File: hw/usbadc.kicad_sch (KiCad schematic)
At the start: 0 parts

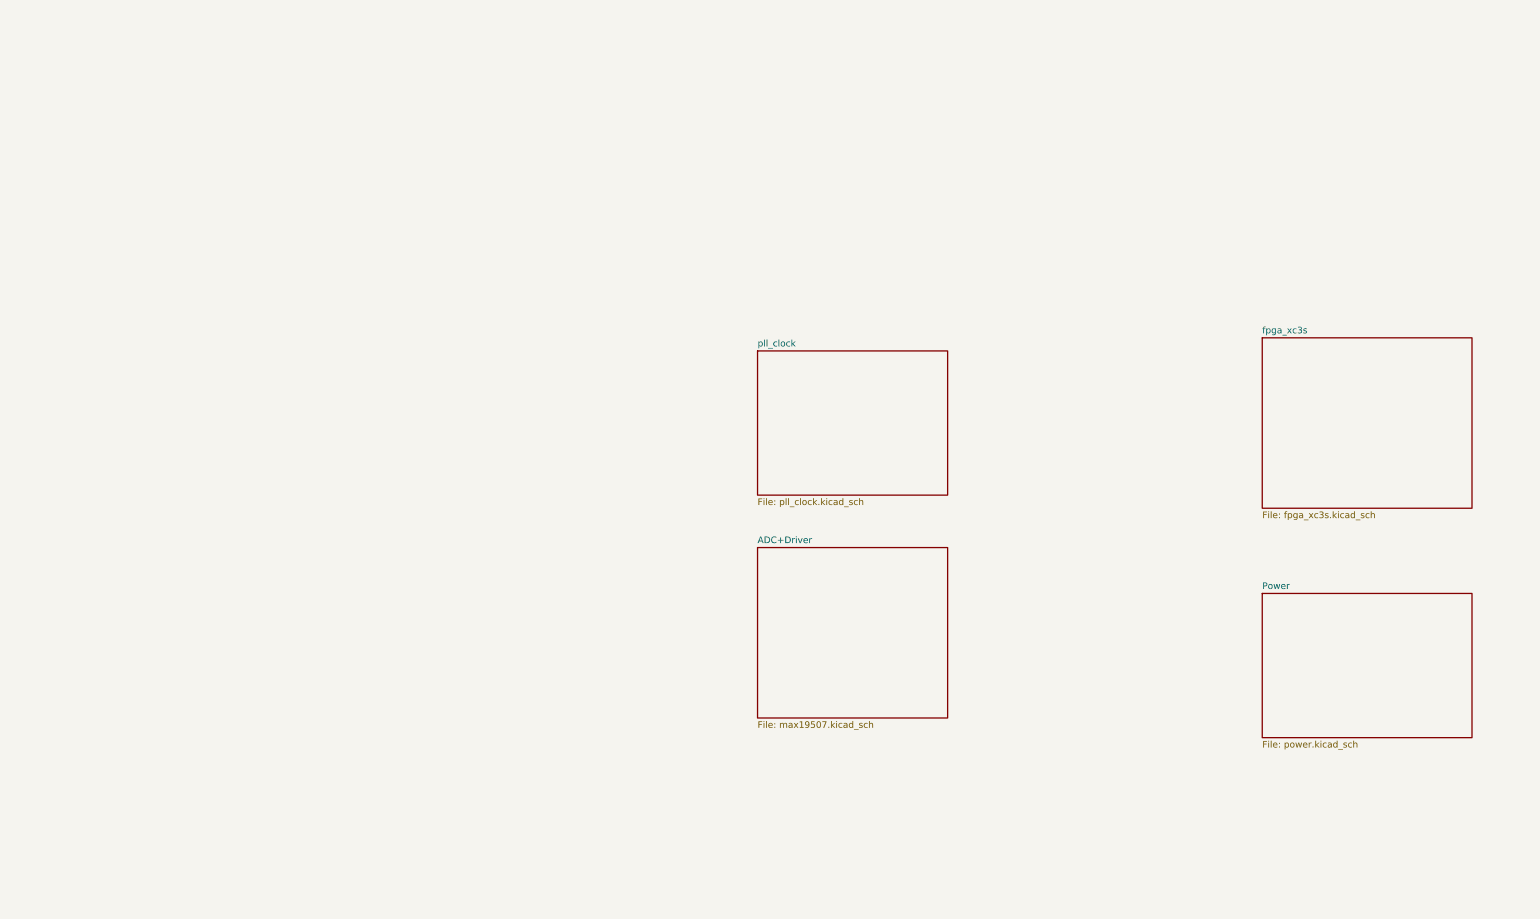
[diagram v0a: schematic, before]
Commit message: basic schematic, started layout (placing first components)
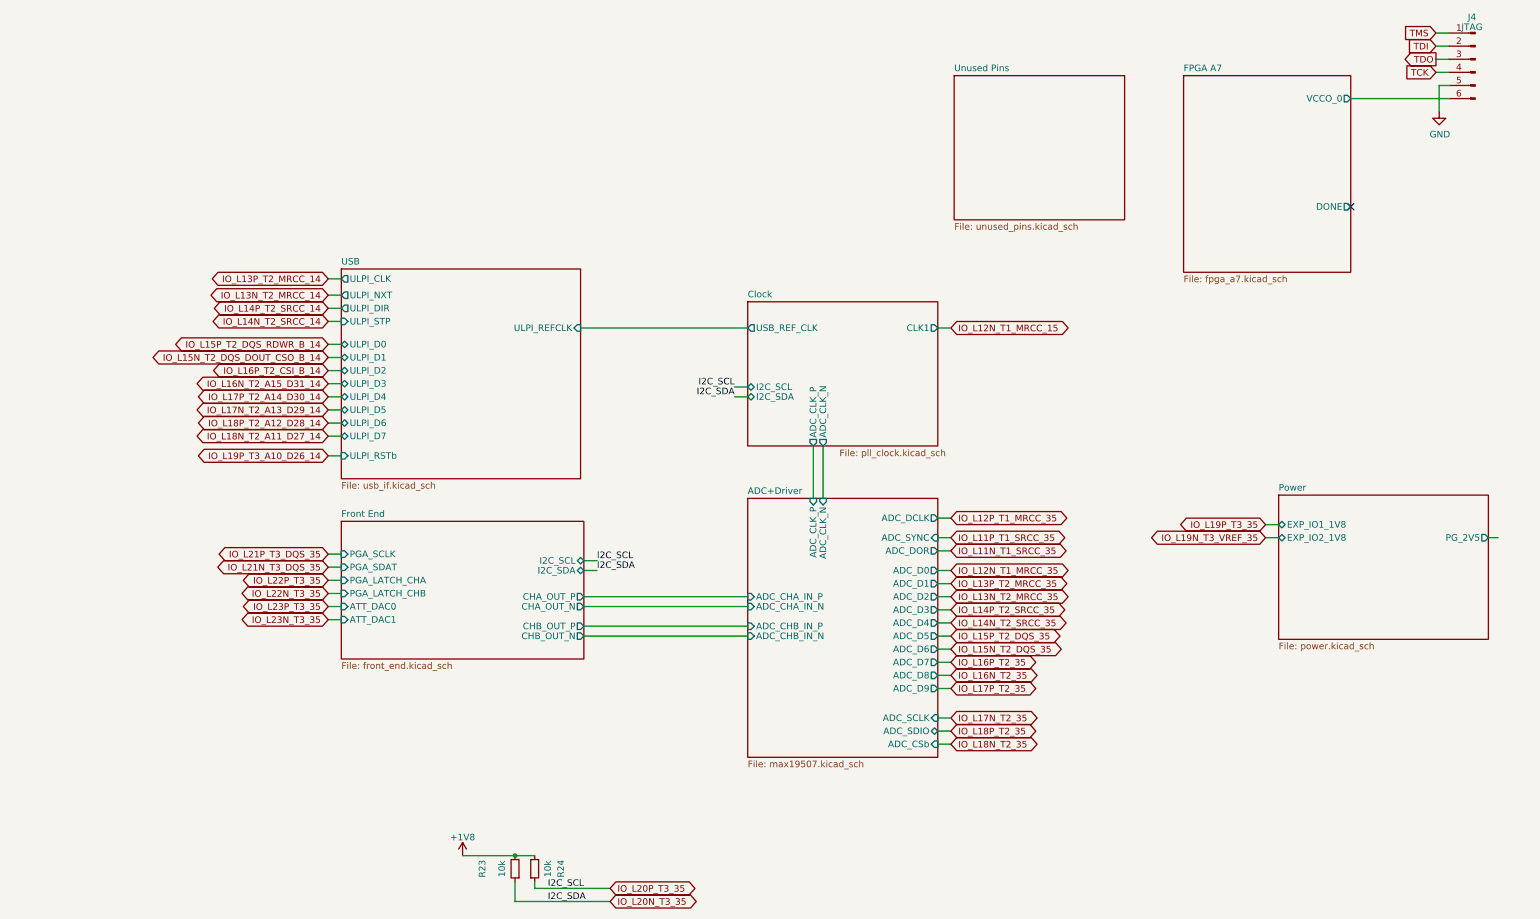
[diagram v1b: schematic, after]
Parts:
- added J4: JTAG, Connector_PinHeader_2.54mm:PinHeader_1x06_P2.54mm_Vertical, symbol Connector:Conn_01x06_Pin
- added R23, R24: 10k, Resistor_SMD:R_0603_1608Metric, symbol Device:R_Small
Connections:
- new net +1V8: R23.2, R24.2
- new net FPGA A7/VCCO_0: J4.6 (Pin_6)
- new net GND: J4.5 (Pin_5)
- new net IO_L20N_T3_35: R23.1
- new net IO_L20P_T3_35: R24.1
- new net TCK: J4.4 (Pin_4)
- new net TDI: J4.2 (Pin_2)
- new net TDO: J4.3 (Pin_3)
- new net TMS: J4.1 (Pin_1)
- no-connect marks 0 -> 1
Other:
- sheet pll_clock renamed Clock
- removed sheet fpga_xc3s
- added sheet FPGA A7 (fpga_a7.kicad_sch)
- added sheet Front End (front_end.kicad_sch)
- added sheet USB (usb_if.kicad_sch)
- added sheet Unused Pins (unused_pins.kicad_sch)
- sheet ADC+Driver ports: added ADC_CHA_IN_N, ADC_CHA_IN_P, ADC_CHB_IN_N, ADC_CHB_IN_P, ADC_CLK_N, ADC_CLK_P, ADC_CSb, ADC_D0, ADC_D1, ADC_D2, ADC_D3, ADC_D4, ADC_D5, ADC_D6, ADC_D7, ADC_D8, ADC_D9, ADC_DCLK, ADC_DOR, ADC_SCLK, ADC_SDIO, ADC_SYNC; removed none
- sheet Clock ports: added ADC_CLK_N, ADC_CLK_P, CLK1, I2C_SCL, I2C_SDA, USB_REF_CLK; removed none
- sheet Power ports: added EXP_IO1_1V8, EXP_IO2_1V8, PG_2V5; removed none

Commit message: WIP (layout)
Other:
- added sheet sheet60F7998F (digio.sch)

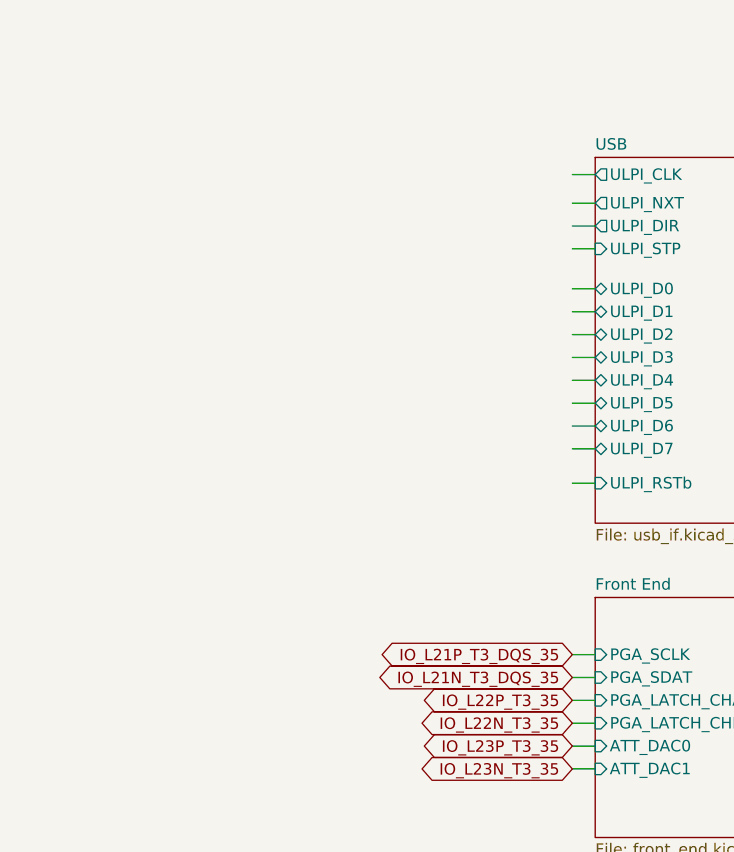
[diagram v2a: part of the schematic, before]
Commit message: connected ulpi PHY
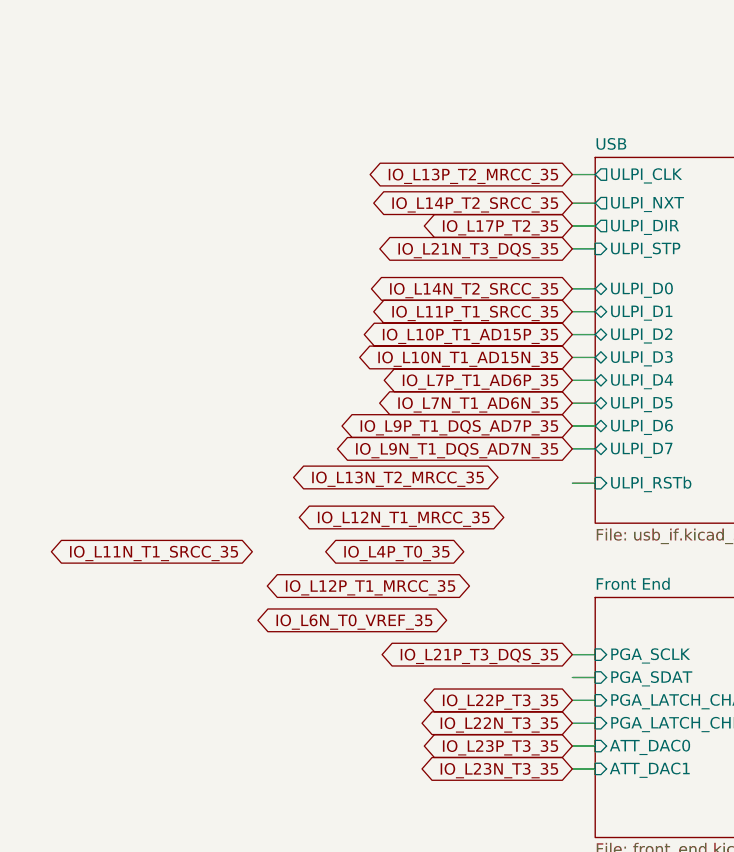
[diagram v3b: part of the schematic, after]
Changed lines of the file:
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@@
+    )
+  )
+  (global_label "IO_L4P_T0_35" (shape bidirectional) (at 38.1 110.49 180) (fields_autoplaced)
+    (effects (font (size 1.27 1.27)) (justify right))
+    (property "Intersheetrefs" "${INTERSHEET_REFS}" (at 21.9541 110.49 0)
+      (effects (font (size 1.27 1.27)) (justify right) hide)
     )
   )
@@
     )
   )
+  (global_label "IO_L9N_T1_DQS_AD7N_35" (shape bidirectional) (at 50.165 99.06 180) (fields_autoplaced)
+    (effects (font (size 1.27 1.27)) (justify right))
+    (property "Intersheetrefs" "${INTERSHEET_REFS}" (at 23.3148 99.06 0)
+      (effects (font (size 1.27 1.27)) (justify right) hide)
+    )
+  )
+  (global_label "IO_L13N_T2_MRCC_35" (shape bidirectional) (at 41.91 102.235 180) (fields_autoplaced)
+    (effects (font (size 1.27 1.27)) (justify right))
+    (property "Intersheetrefs" "${INTERSHEET_REFS}" (at 18.2651 102.235 0)
+      (effects (font (size 1.27 1.27)) (justify right) hide)
+    )
+  )
+  (global_label "IO_L9P_T1_DQS_AD7P_35" (shape bidirectional) (at 50.165 96.52 180) (fields_autoplaced)
+    (effects (font (size 1.27 1.27)) (justify right))
+    (property "Intersheetrefs" "${INTERSHEET_REFS}" (at 23.4358 96.52 0)
+      (effects (font (size 1.27 1.27)) (justify right) hide)
+    )
+  )
   (global_label "IO_L18P_T2_35" (shape bidirectional) (at 170.815 156.21 0) (fields_autoplaced)
     (effects (font (size 1.27 1.27)) (justify left))
@@
     )
   )
-  (global_label "IO_L21N_T3_DQS_35" (shape bidirectional) (at 50.165 124.46 180) (fields_autoplaced)
-    (effects (font (size 1.27 1.27)) (justify right))
-    (property "Intersheetrefs" "${INTERSHEET_REFS}" (at 27.9715 124.46 0)
+  (global_label "IO_L11N_T1_SRCC_35" (shape bidirectional) (at 14.605 110.49 180) (fields_autoplaced)
+    (effects (font (size 1.27 1.27)) (justify right))
+    (property "Intersheetrefs" "${INTERSHEET_REFS}" (at -8.798 110.49 0)
+      (effects (font (size 1.27 1.27)) (justify right) hide)
+    )
+  )
+  (global_label "IO_L21N_T3_DQS_35" (shape bidirectional) (at 50.165 76.835 180) (fields_autoplaced)
+    (effects (font (size 1.27 1.27)) (justify right))
+    (property "Intersheetrefs" "${INTERSHEET_REFS}" (at 27.9715 76.835 0)
+      (effects (font (size 1.27 1.27)) (justify right) hide)
+    )
+  )
+  (global_label "IO_L13P_T2_MRCC_35" (shape bidirectional) (at 50.165 68.58 180) (fields_autoplaced)
+    (effects (font (size 1.27 1.27)) (justify right))
+    (property "Intersheetrefs" "${INTERSHEET_REFS}" (at 26.5806 68.58 0)
+      (effects (font (size 1.27 1.27)) (justify right) hide)
+    )
+  )
+  (global_label "IO_L12P_T1_MRCC_35" (shape bidirectional) (at 38.735 114.3 180) (fields_autoplaced)
+    (effects (font (size 1.27 1.27)) (justify right))
+    (property "Intersheetrefs" "${INTERSHEET_REFS}" (at 15.1506 114.3 0)
       (effects (font (size 1.27 1.27)) (justify right) hide)
     )
@@
     )
   )
+  (global_label "IO_L10P_T1_AD15P_35" (shape bidirectional) (at 50.165 86.36 180) (fields_autoplaced)
+    (effects (font (size 1.27 1.27)) (justify right))
+    (property "Intersheetrefs" "${INTERSHEET_REFS}" (at 25.7944 86.36 0)
+      (effects (font (size 1.27 1.27)) (justify right) hide)
+    )
+  )
   (global_label "IO_L19P_T3_35" (shape bidirectional) (at 231.775 116.205 180) (fields_autoplaced)
     (effects (font (size 1.27 1.27)) (justify right))
@@
     )
   )
+  (global_label "IO_L11P_T1_SRCC_35" (shape bidirectional) (at 50.165 83.82 180) (fields_autoplaced)
+    (effects (font (size 1.27 1.27)) (justify right))
+    (property "Intersheetrefs" "${INTERSHEET_REFS}" (at 26.8225 83.82 0)
+      (effects (font (size 1.27 1.27)) (justify right) hide)
+    )
+  )
+  (global_label "IO_L14P_T2_SRCC_35" (shape bidirectional) (at 50.165 71.755 180) (fields_autoplaced)
+    (effects (font (size 1.27 1.27)) (justify right))
+    (property "Intersheetrefs" "${INTERSHEET_REFS}" (at 26.8225 71.755 0)
+      (effects (font (size 1.27 1.27)) (justify right) hide)
+    )
+  )
+  (global_label "IO_L7N_T1_AD6N_35" (shape bidirectional) (at 50.165 93.98 180) (fields_autoplaced)
+    (effects (font (size 1.27 1.27)) (justify right))
+    (property "Intersheetrefs" "${INTERSHEET_REFS}" (at 28.0924 93.98 0)
+      (effects (font (size 1.27 1.27)) (justify right) hide)
+    )
+  )
   (global_label "IO_L17P_T2_A26_15" (shape bidirectional) (at 205.74 146.05 0) (fields_autoplaced)
     (effects (font (size 1.27 1.27)) (justify left))
@@
     )
   )
+  (global_label "IO_L12N_T1_MRCC_35" (shape bidirectional) (at 42.545 106.68 180) (fields_autoplaced)
+    (effects (font (size 1.27 1.27)) (justify right))
+    (property "Intersheetrefs" "${INTERSHEET_REFS}" (at 18.9001 106.68 0)
+      (effects (font (size 1.27 1.27)) (justify right) hide)
+    )
+  )
   (global_label "TDO" (shape output) (at 264.795 26.035 180) (fields_autoplaced)
     (effects (font (size 1.27 1.27)) (justify right))
@@
     )
   )
+  (global_label "IO_L6N_T0_VREF_35" (shape bidirectional) (at 36.195 118.11 180) (fields_autoplaced)
+    (effects (font (size 1.27 1.27)) (justify right))
+    (property "Intersheetrefs" "${INTERSHEET_REFS}" (at 14.4248 118.11 0)
+      (effects (font (size 1.27 1.27)) (justify right) hide)
+    )
+  )
   (global_label "IO_L22P_T3_35" (shape bidirectional) (at 50.165 127 180) (fields_autoplaced)
     (effects (font (size 1.27 1.27)) (justify right))
@@
     )
   )
+  (global_label "IO_L14N_T2_SRCC_35" (shape bidirectional) (at 50.165 81.28 180) (fields_autoplaced)
+    (effects (font (size 1.27 1.27)) (justify right))
+    (property "Intersheetrefs" "${INTERSHEET_REFS}" (at 26.762 81.28 0)
+      (effects (font (size 1.27 1.27)) (justify right) hide)
+    )
+  )
   (global_label "IO_L15N_T2_DQS_ADV_B_15" (shape bidirectional) (at 170.815 127.635 0) (fields_autoplaced)
     (effects (font (size 1.27 1.27)) (justify left))
@@
     )
   )
+  (global_label "IO_L7P_T1_AD6P_35" (shape bidirectional) (at 50.165 91.44 180) (fields_autoplaced)
+    (effects (font (size 1.27 1.27)) (justify right))
+    (property "Intersheetrefs" "${INTERSHEET_REFS}" (at 28.2134 91.44 0)
+      (effects (font (size 1.27 1.27)) (justify right) hide)
+    )
+  )
   (global_label "IO_L13N_T2_MRCC_15" (shape bidirectional) (at 208.915 136.525 0) (fields_autoplaced)
     (effects (font (size 1.27 1.27)) (justify left))
@@
     )
   )
+  (global_label "IO_L10N_T1_AD15N_35" (shape bidirectional) (at 50.165 88.9 180) (fields_autoplaced)
+    (effects (font (size 1.27 1.27)) (justify right))
+    (property "Intersheetrefs" "${INTERSHEET_REFS}" (at 25.6734 88.9 0)
+      (effects (font (size 1.27 1.27)) (justify right) hide)
+    )
+  )
   (global_label "IO_L15P_T2_DQS_15" (shape bidirectional) (at 200.66 162.56 0) (fields_autoplaced)
     (effects (font (size 1.27 1.27)) (justify left))
@@
       (effects (font (size 1.27 1.27)) (justify right) hide)
     )
+  )
+  (global_label "IO_L17P_T2_35" (shape bidirectional) (at 50.165 74.295 180) (fields_autoplaced)
+    (effects (font (size 1.27 1.27)) (justify right))
+    (property "Intersheetrefs" "${INTERSHEET_REFS}" (at 32.8096 74.295 0)
+      (effects (font (size 1.27 1.27)) (justify right) hide)
+    )

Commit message: WIP - a lot already laid out.
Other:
- added sheet LEDs (leds.kicad_sch)
- sheet Front End ports: added none; removed ATT_DAC0, ATT_DAC1
- sheet sheet60F7998F: file digio.sch -> digio.kicad_sch
